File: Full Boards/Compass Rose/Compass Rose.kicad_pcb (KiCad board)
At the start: 4 copper layers, 170 x 180 mm, 247 parts, among them J1 Program Header, J3 Optional Bond, Q1 BSS314PE, Q2 DMN6075S, Q3 BSS314PE, Q4 DMN6075S, Q5 BSS314PE, Q6 DMN6075S, SW1 Boot, SW2 Reset, SW3 CTS_219-2MSTR

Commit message: Finished the first refactored PCB layout.
Signed-off-by: digimer <digital.mermaid@gmail.com>
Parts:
- removed TP2: Iso Power, Connector_PinHeader_2.54mm:PinHeader_1x02_P2.54mm_Vertical
- removed TP3: Board Power, Connector_PinHeader_2.54mm:PinHeader_1x03_P2.54mm_Vertical
- moved C15 103.5 mm to (188.8, 104.5), turned to -90 degrees
- moved C14 101.5 mm to (191.1, 104.0), turned to 90 degrees
- moved C16 98.0 mm to (193.3, 104.5), turned to -90 degrees
- moved R21 86.4 mm to (221.2, 107.8)
- moved R22 86.4 mm to (221.2, 111.0)
- moved R3 86.4 mm to (216.6, 111.0)
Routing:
- net /NRST: track 179.8 -> 190.0 mm, vias 4 -> 5
- net GND: track 91.0 -> 100.5 mm, vias 76 -> 77
- net /USART1_TX: track 133.4 -> 141.8 mm
- net /USART1_RX: track 134.1 -> 141.8 mm
- net +3.3V: track 60.1 -> 66.1 mm, vias 20 -> 19

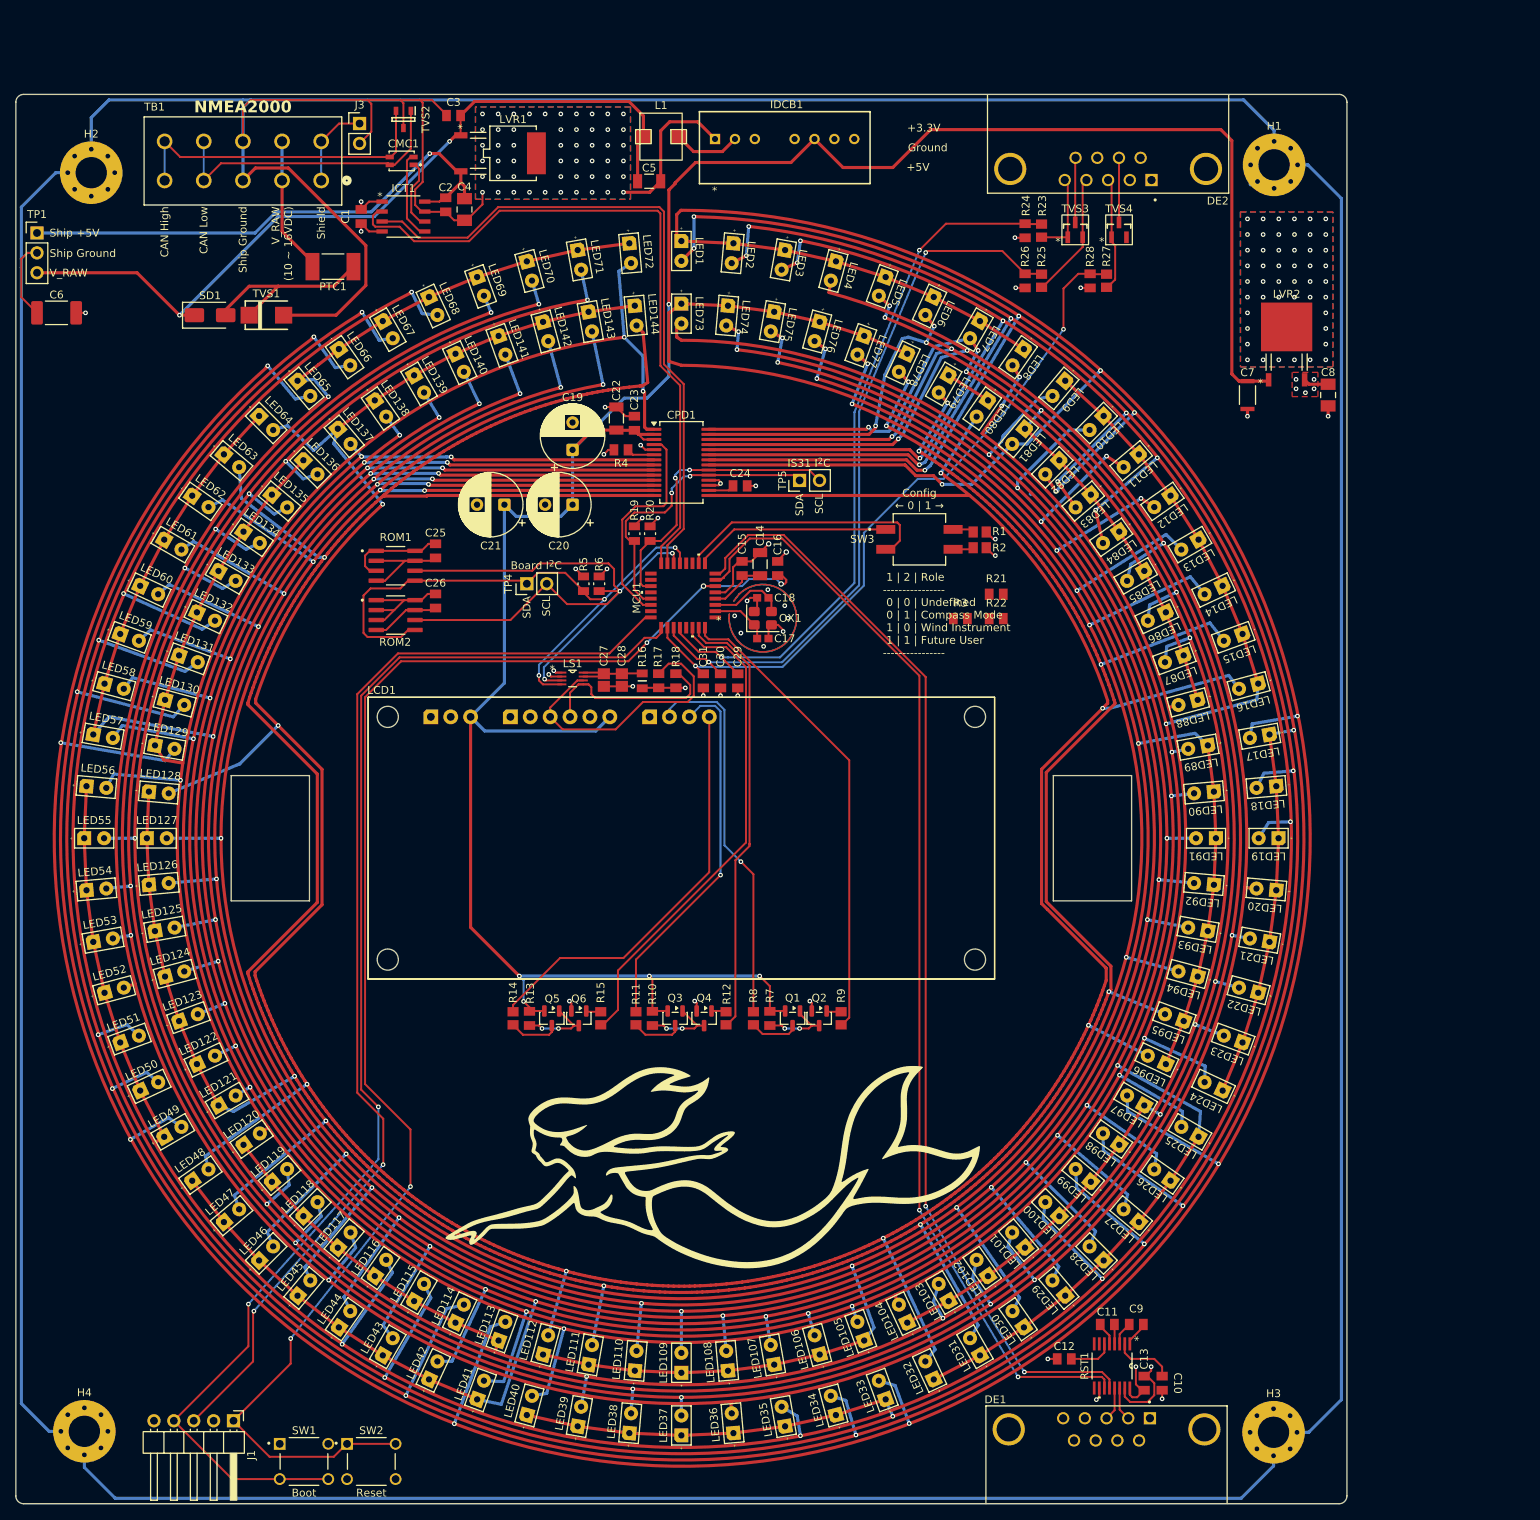
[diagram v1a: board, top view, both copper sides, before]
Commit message: Routed missed resistors.
Signed-off-by: digimer <digital.mermaid@gmail.com>
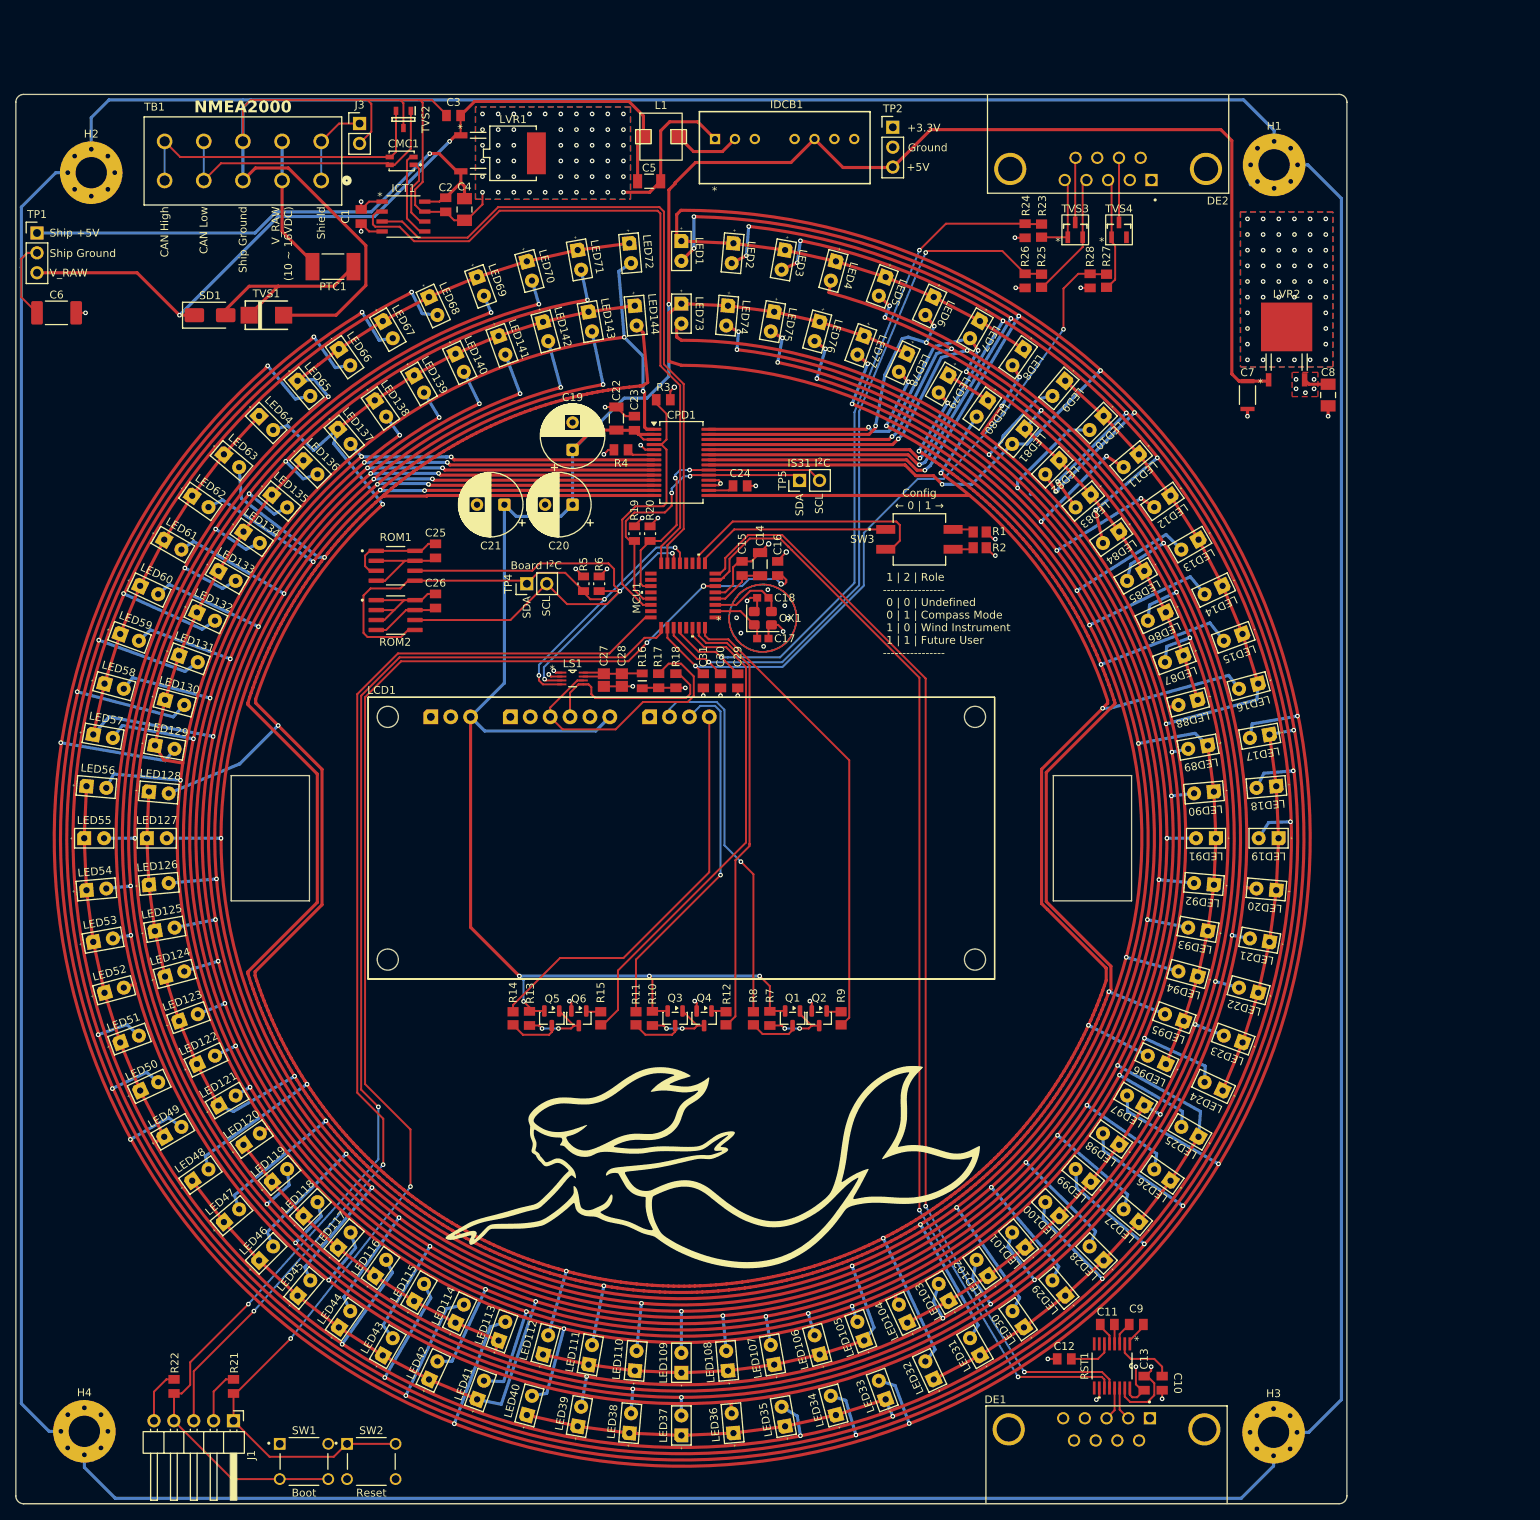
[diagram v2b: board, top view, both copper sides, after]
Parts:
- added TP2: Board Power, Connector_PinHeader_2.54mm:PinHeader_1x03_P2.54mm_Vertical, F.Cu at (208.0, 48.2)
- moved R22 143.7 mm to (116.2, 209.0), turned to 90 degrees
- moved R21 140.4 mm to (123.8, 209.0), turned to 90 degrees
- moved R3 47.1 mm to (178.7, 83.0)
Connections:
- R22 pad 1: GND -> /DEBUG_SWCLK
- R22 pad 2: /DEBUG_SWCLK -> GND
- R3 pad 1: +3.3V -> /IS31_INTB_OUT
- R3 pad 2: /IS31_INTB_OUT -> +3.3V
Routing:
- net +3.3V: track 66.1 -> 74.9 mm, vias 19 -> 20
- net GND: track 100.5 -> 107.4 mm
- net /IS31_INTB_OUT: track 28.2 -> 34.7 mm
- net /DEBUG_SWCLK: track 168.9 -> 169.5 mm
- added copper zone on In2.Cu, net GND
